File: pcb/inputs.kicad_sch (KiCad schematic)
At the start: 84 parts, among them SW1 SW_Push

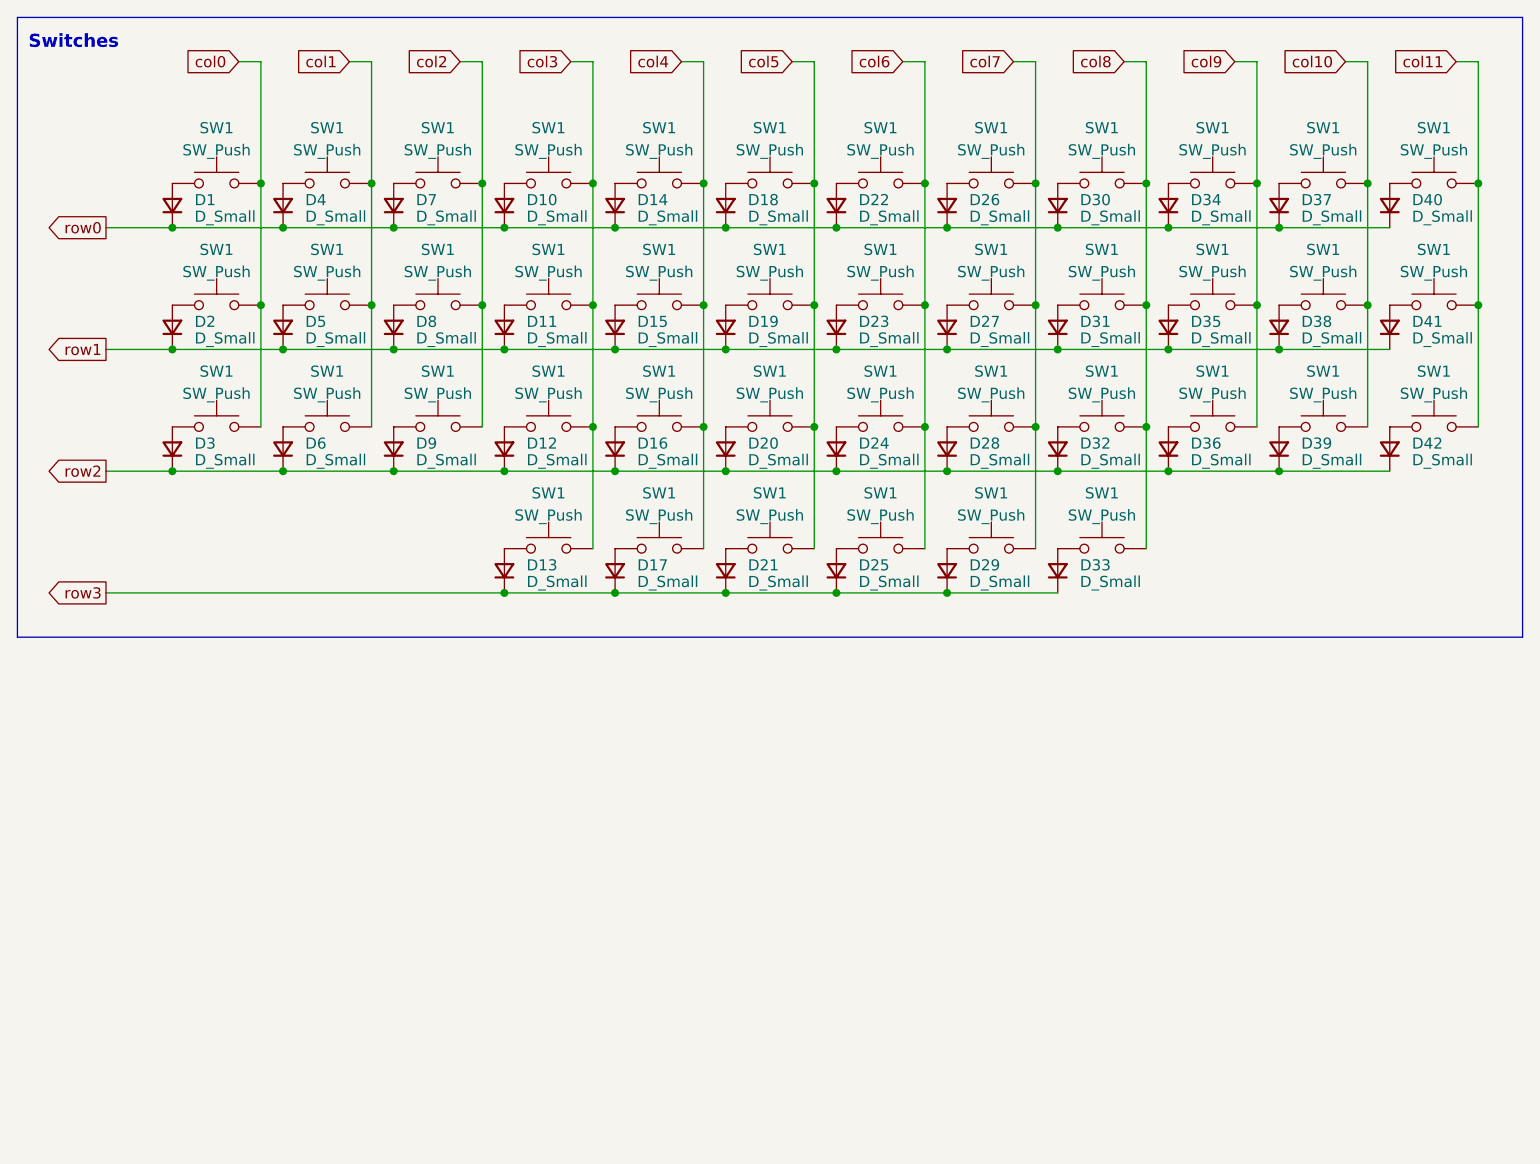
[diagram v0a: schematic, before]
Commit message: Finished off schematic
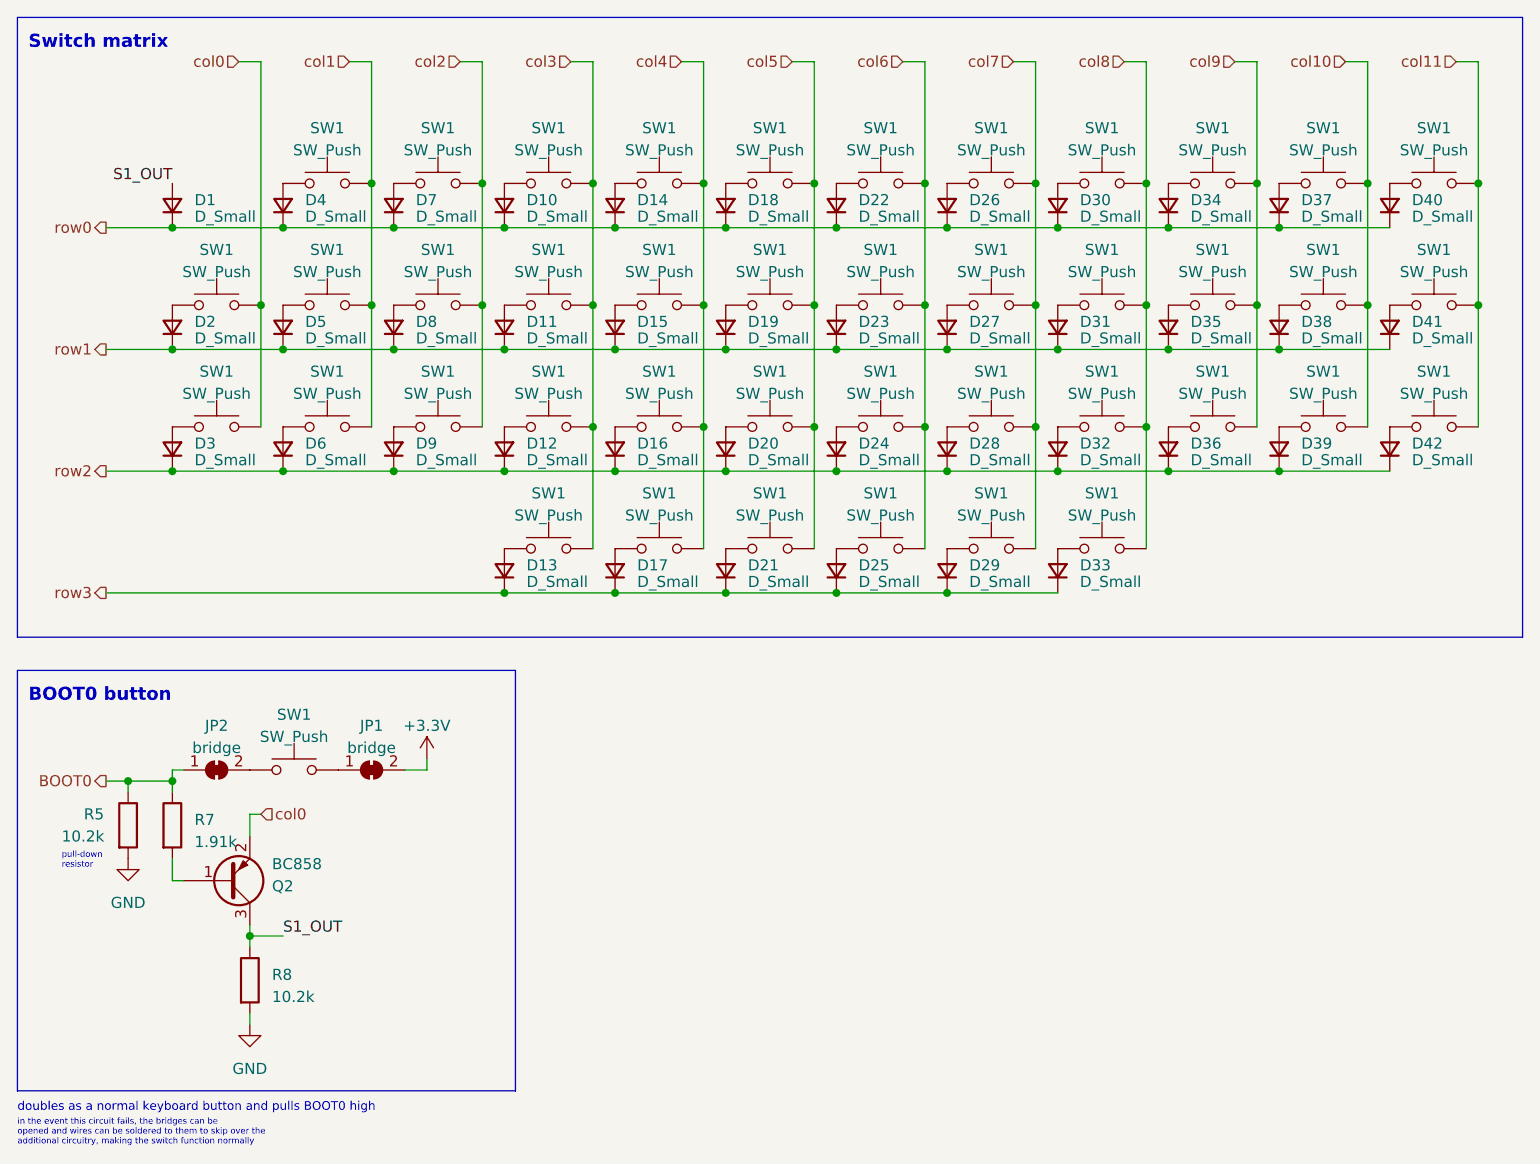
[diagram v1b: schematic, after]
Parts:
- added JP1, JP2: bridge, Jumper:SolderJumper-2_P1.3mm_Open_RoundedPad1.0x1.5mm, symbol Jumper:SolderJumper_2_Bridged
- added Q2: BC858, Package_TO_SOT_SMD:SOT-23, symbol Transistor_BJT:BC858
- added R5, R8: 10.2k, Resistor_SMD:R_0201_0603Metric, symbol Device:R
- added R7: 1.91k, Resistor_SMD:R_0201_0603Metric, symbol Device:R
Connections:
- net col0: now also Q2.2 (E); no longer SW1.2
- net at SW1.1: now also JP2.2 (B); no longer D1.2 (A)
- new net: JP1.1 (A), SW1.2
- new net: Q2.1 (B), R7.2
- new net +3.3V: JP1.2 (B)
- new net BOOT0: JP2.1 (A), R5.1, R7.1
- new net GND: R5.2, R8.2
- new net S1_OUT: D1.2 (A), Q2.3 (C), R8.1
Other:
- note added: "BOOT0 button"
- note added: "Switch matrix"
- note added: "doubles as a normal keyboard button and pulls BOOT0 high"
- note added: "in the event this circuit fails, the bridges can be opened and wires can be soldered to them to skip over the additional circuitry, making the switch function normally"
- note added: "pull-down resistor"
- note removed: "Switches"

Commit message: Finished routing, ready for checks
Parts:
- added C20: 0.1u, Capacitor_SMD:C_0603_1608Metric, symbol Device:C_Small
- added SW2: TS-1187A-B-A-B, Button_Switch_SMD:SW_Push_1P1T_NO_CK_KSC6xxJ, symbol Switch:SW_Push
- R5, R7, R8: footprint Resistor_SMD:R_0201_0603Metric -> Resistor_SMD:R_0603_1608Metric
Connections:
- net GND: now also C20.2, SW2.1
- new net NRST: C20.1, SW2.2
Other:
- note added: "Reset button"
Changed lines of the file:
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@@
   (junction (at 93.98 49.53) (diameter 0) (color 0 0 0 0)
   )
+  (junction (at 91.44 118.11) (diameter 0) (color 0 0 0 0)
+  )
   (junction (at 106.68 63.5) (diameter 0) (color 0 0 0 0)
   )
@@
   (junction (at 106.68 77.47) (diameter 0) (color 0 0 0 0)
   )
+  (junction (at 104.14 114.3) (diameter 0) (color 0 0 0 0)
+  )
   (junction (at 43.18 77.47) (diameter 0) (color 0 0 0 0)
   )
@@
     (stroke (width 0) (type default))
   )
+  (wire (pts (xy 104.14 114.3) (xy 102.87 114.3))
+    (stroke (width 0) (type default))
+  )
   (wire (pts (xy 35.56 77.47) (xy 43.18 77.47))
     (stroke (width 0) (type default))
@@
     (stroke (width 0) (type default))
   )
+  (wire (pts (xy 100.33 118.11) (xy 104.14 118.11))
+    (stroke (width 0) (type default))
+  )
   (wire (pts (xy 81.28 91.44) (xy 93.98 91.44))
     (stroke (width 0) (type default))
   )
+  (wire (pts (xy 91.44 114.3) (xy 91.44 118.11))
+    (stroke (width 0) (type default))
+  )
+  (wire (pts (xy 91.44 118.11) (xy 95.25 118.11))
+    (stroke (width 0) (type default))
+  )
   (wire (pts (xy 142.24 58.42) (xy 142.24 72.39))
     (stroke (width 0) (type default))
@@
     (stroke (width 0) (type default))
   )
+  (wire (pts (xy 104.14 114.3) (xy 105.41 114.3))
+    (stroke (width 0) (type default))
+  )
   (wire (pts (xy 43.18 77.47) (xy 55.88 77.47))
     (stroke (width 0) (type default))
@@
     (stroke (width 0) (type default))
   )
+  (wire (pts (xy 104.14 118.11) (xy 104.14 114.3))
+    (stroke (width 0) (type default))
+  )
   (wire (pts (xy 104.14 72.39) (xy 104.14 86.36))
     (stroke (width 0) (type default))
@@
     (stroke (width 0) (type default))
   )
+  (wire (pts (xy 91.44 118.11) (xy 91.44 119.38))
+    (stroke (width 0) (type default))
+  )
   (wire (pts (xy 52.07 130.81) (xy 52.07 132.08))
     (stroke (width 0) (type default))
@@
     (stroke (width 0) (type default))
   )
+  (wire (pts (xy 92.71 114.3) (xy 91.44 114.3))
+    (stroke (width 0) (type default))
+  )
   (wire (pts (xy 116.84 30.48) (xy 116.84 44.45))
     (stroke (width 0) (type default))
@@
   (wire (pts (xy 91.44 72.39) (xy 91.44 86.36))
     (stroke (width 0) (type default))
+  )
+  (rectangle (start 86.36 100.33) (end 114.3 127)
+    (stroke (width 0) (type default))
+    (fill (type none))
   )
   (rectangle (start 25.4 100.33) (end 82.55 148.59)
@@
     (effects (font (size 1.5 1.5) (thickness 0.254) bold) (justify left bottom))
   )
+  (text "Reset button" (at 87.63 104.14 0)
+    (effects (font (size 1.5 1.5) (thickness 0.254) bold) (justify left bottom))
+  )
   (text "pull-down\nresistor" (at 30.48 123.19 0)
     (effects (font (size 0.7 0.7)) (justify left bottom))
@@
     (effects (font (size 1.27 1.27)) (justify right))
   )
+  (hierarchical_label "NRST" (shape output) (at 105.41 114.3 0) (fields_autoplaced)
+    (effects (font (size 1.27 1.27)) (justify left))
+  )
   (hierarchical_label "row3" (shape output) (at 35.56 91.44 180) (fields_autoplaced)
     (effects (font (size 1.27 1.27)) (justify right))
@@
         (path "/fc529d87-72d0-4c92-b352-ddcf4c6f7199/1c8ac5bd-b3bc-4835-a71b-e635010cd696"
           (reference "D33") (unit 1)
+        )
+      )
+    )
+  )
+  (symbol (lib_id "power:GND") (at 91.44 119.38 0) (unit 1)
+    (in_bom yes) (on_board yes) (dnp no)
+    (property "Reference" "#PWR047" (at 91.44 125.73 0)
+      (effects (font (size 1.27 1.27)) hide)
+    )
+    (property "Value" "GND" (at 91.44 123.19 0)
+      (effects (font (size 1.27 1.27)))
+    )
+    (property "Footprint" "" (at 91.44 119.38 0)
+      (effects (font (size 1.27 1.27)) hide)
+    )
+    (property "Datasheet" "" (at 91.44 119.38 0)
+      (effects (font (size 1.27 1.27)) hide)
+    )
+    (pin "1")
+    (instances
+      (project "neptune"
+        (path "/e63e39d7-6ac0-4ffd-8aa3-1841a4541b55/708c8a34-f258-4554-8b50-7818f1e46fec"
+          (reference "#PWR047") (unit 1)
+        )
+      )
+      (project "keyboard"
+        (path "/fc529d87-72d0-4c92-b352-ddcf4c6f7199/1c8ac5bd-b3bc-4835-a71b-e635010cd696"
+          (reference "#PWR036") (unit 1)
         )
       )
@@
         (path "/fc529d87-72d0-4c92-b352-ddcf4c6f7199/1c8ac5bd-b3bc-4835-a71b-e635010cd696"
           (reference "SW19") (unit 1)
+        )
+      )
+    )
+  )
+  (symbol (lib_id "Device:C_Small") (at 97.79 118.11 270) (unit 1)
+    (in_bom yes) (on_board yes) (dnp no)
+    (property "Reference" "C20" (at 97.79 121.92 90)
+      (effects (font (size 1.27 1.27)))
+    )
+    (property "Value" "0.1u" (at 97.79 124.46 90)
+      (effects (font (size 1.27 1.27)))
+    )
+    (property "Footprint" "Capacitor_SMD:C_0603_1608Metric" (at 97.79 118.11 0)
+      (effects (font (size 1.27 1.27)) hide)
+    )
+    (property "Datasheet" "~" (at 97.79 118.11 0)
+      (effects (font (size 1.27 1.27)) hide)
+    )
+    (pin "1")
+    (pin "2")
+    (instances
+      (project "neptune"
+        (path "/e63e39d7-6ac0-4ffd-8aa3-1841a4541b55/708c8a34-f258-4554-8b50-7818f1e46fec"
+          (reference "C20") (unit 1)
+        )
+      )
+      (project "keyboard"
+        (path "/fc529d87-72d0-4c92-b352-ddcf4c6f7199/1c8ac5bd-b3bc-4835-a71b-e635010cd696"
+          (reference "C17") (unit 1)
         )
       )
@@
       (effects (font (size 1.27 1.27)) (justify left))
     )
-    (property "Footprint" "Resistor_SMD:R_0201_0603Metric" (at 41.402 118.11 90)
+    (property "Footprint" "Resistor_SMD:R_0603_1608Metric" (at 41.402 118.11 90)
       (effects (font (size 1.27 1.27)) hide)
     )
@@
         (path "/fc529d87-72d0-4c92-b352-ddcf4c6f7199/1c8ac5bd-b3bc-4835-a71b-e635010cd696"
           (reference "SW10") (unit 1)
+        )
+      )
+    )
+  )
+  (symbol (lib_id "Switch:SW_Push") (at 97.79 114.3 0) (unit 1)
+    (in_bom yes) (on_board yes) (dnp no)
+    (property "Reference" "SW2" (at 97.79 107.315 0)
+      (effects (font (size 1.27 1.27)))
+    )
+    (property "Value" "TS-1187A-B-A-B" (at 97.79 109.855 0)
+      (effects (font (size 1.27 1.27)))
+    )
+    (property "Footprint" "Button_Switch_SMD:SW_Push_1P1T_NO_CK_KSC6xxJ" (at 97.79 109.22 0)
+      (effects (font (size 1.27 1.27)) hide)
+    )
+    (property "Datasheet" "~" (at 97.79 109.22 0)
+      (effects (font (size 1.27 1.27)) hide)
+    )
+    (property "LCSC" "C318884" (at 97.79 114.3 0)
+      (effects (font (size 1.27 1.27)) hide)
+    )
+    (pin "1")
+    (pin "2")
+    (instances
+      (project "neptune"
+        (path "/e63e39d7-6ac0-4ffd-8aa3-1841a4541b55/708c8a34-f258-4554-8b50-7818f1e46fec"
+          (reference "SW2") (unit 1)
+        )
+      )
+      (project "keyboard"
+        (path "/fc529d87-72d0-4c92-b352-ddcf4c6f7199/1c8ac5bd-b3bc-4835-a71b-e635010cd696"
+          (reference "SW43") (unit 1)
         )
       )
@@
       (effects (font (size 1.27 1.27)) (justify left))
     )
-    (property "Footprint" "Resistor_SMD:R_0201_0603Metric" (at 36.322 118.11 90)
+    (property "Footprint" "Resistor_SMD:R_0603_1608Metric" (at 36.322 118.11 90)
       (effects (font (size 1.27 1.27)) hide)
     )
@@
       (effects (font (size 1.27 1.27)) (justify left))
     )
-    (property "Footprint" "Resistor_SMD:R_0201_0603Metric" (at 50.292 135.89 90)
-      (effects (font (size 1.27 1.27)) hide)
-    )
+    (property "Footprint" "Resistor_SMD:R_0603_1608Metric" (at 50.292 135.89 90)
+      (effects (font (size 1.27 1.27)) hide)
+    )
